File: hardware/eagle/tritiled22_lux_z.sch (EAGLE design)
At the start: 15 parts, among them Q1 ZXMN3B01FTA, Q2 DMG2305UX, SW1 SMD_SWITCH, U1 PIC12LF1571

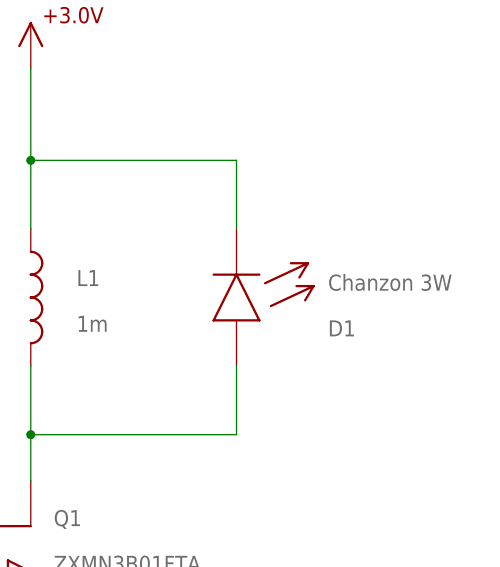
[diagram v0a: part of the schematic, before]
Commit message: Added new LED eiditons: 5630, Luxeon C, Luxeon Z fixed inconsistent C2 value: now should be 100n everywhere
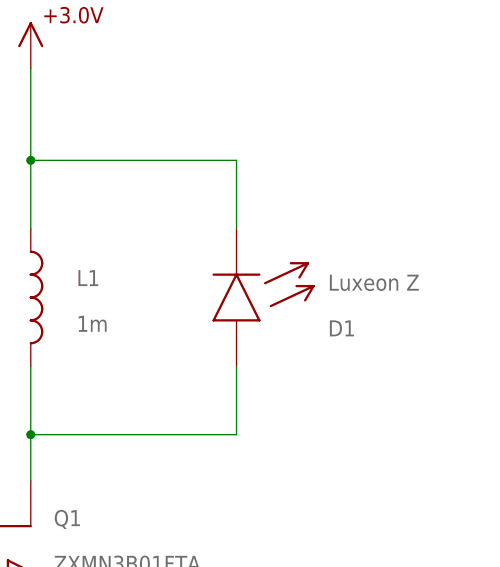
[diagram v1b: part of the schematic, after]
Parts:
- D1: value Chanzon 3W -> Luxeon Z; device tritiled:LED_3W -> tritiled:LEDLUXEON_Z
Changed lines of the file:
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@@
 <part name="U$8" library="z0" deviceset="GND" device=""/>
 <part name="U$11" library="z0" deviceset="GND" device=""/>
-<part name="D1" library="tritiled" deviceset="LED_3W" device="" value="Chanzon 3W"/>
+<part name="D1" library="tritiled" deviceset="LED" device="LUXEON_Z" value="Luxeon Z"/>
 <part name="L1" library="tritiled" deviceset="SRR6028_INDUCTOR" device="" value="1m"/>
 <part name="U$13" library="tritiled" deviceset="+3.0V" device=""/>
